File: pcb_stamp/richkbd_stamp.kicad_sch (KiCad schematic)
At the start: 48 parts, among them J1 USB_C_Receptacle, J2 OLED, K0 key-diode-led, K1 key-diode-led, K10 key-diode-led, K100 key-diode-led, K101 key-diode-led, K102 key-diode-led, K11 key-diode-led, K110 key-diode-led, K111 key-diode-led, K112 key-diode-led, K12 key-diode-led, K2 key-diode-led, K20 key-diode-led, K21 key-diode-led, K22 key-diode-led, K30 key-diode-led, K31 key-diode-led, K32 key-diode-led, K33 key-diode-led, K40 key-diode-led, K41 key-diode-led, K42 key-diode-led, K43 key-diode-led, K50 key-diode-led, K51 key-diode-led, K52 key-diode-led, K53 key-diode-led, K60 key-diode-led, K61 key-diode-led, K62 key-diode-led, K63 key-diode-led, K70 key-diode-led, K71 key-diode-led, K72 key-diode-led, K73 key-diode-led, K80 key-diode-led, K81 key-diode-led, K82 key-diode-led, K83 key-diode-led, K90 key-diode-led, K91 key-diode-led, K92 key-diode-led, U1 RP2040_Stamp

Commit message: Finished stamp routing
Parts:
- removed J1: USB_C_Receptacle, symbol Connector:USB_C_Receptacle
- added J1: USB_C_Receptacle_USB2.0, Connector_USB:USB_C_Receptacle_GCT_USB4085, symbol Connector:USB_C_Receptacle_USB2.0
- added R3, R4: R, Resistor_SMD:R_0805_2012Metric, symbol Device:R
- R1, R2: footprint kbd:R -> Resistor_SMD:R_0805_2012Metric
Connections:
- net GND: now also J1.A1 (GND), J1.A12 (GND), J1.B1 (GND), J1.B12 (GND), J1.S1 (SHIELD), R3.1, R4.1
- net LED: now also U1.15 (GPIO14)
- net SCL: now also U1.2 (GPIO1)
- net SDA: now also U1.1 (GPIO0)
- net VCC: now also J1.A4 (VBUS), J1.A9 (VBUS), J1.B4 (VBUS), J1.B9 (VBUS)
- net col0: now also U1.11 (GPIO10)
- net col1: now also U1.10 (GPIO9)
- net col10: now also U1.22 (GPIO21)
- net col11: now also U1.21 (GPIO20)
- net col2: now also U1.9 (GPIO8)
- net col3: now also U1.8 (GPIO7)
- net col4: now also U1.7 (GPIO6)
- net col5: now also U1.6 (GPIO5)
- net col6: now also U1.26 (GPIO25)
- net col7: now also U1.25 (GPIO24)
- net col8: now also U1.24 (GPIO23)
- net col9: now also U1.23 (GPIO22)
- net row0: now also U1.3 (GPIO2)
- net row1: now also U1.4 (GPIO3)
- net row2: now also U1.5 (GPIO4)
- net at U1.36 (USB_D+): now also J1.A6 (D+), J1.B6 (D+)
- net at U1.35 (USB_D-): now also J1.A7 (D-), J1.B7 (D-)
- new net CC1: J1.A5 (CC1), R3.2
- new net CC2: J1.B5 (CC2), R4.2
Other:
- moved on the sheet: J2, R1, R2, RSW1, U1

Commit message: Moved OLED up and fixed pin orientation
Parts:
- RSW1: value RESET -> BOOTSEL
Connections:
- net reset renamed bootsel
- no-connect marks 2 -> 21
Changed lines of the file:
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@@
   (junction (at 186.69 109.22) (diameter 0) (color 0 0 0 0)
   )
+  (no_connect (at 271.78 92.71))
+  (no_connect (at 271.78 95.25))
+  (no_connect (at 271.78 97.79))
+  (no_connect (at 271.78 100.33))
+  (no_connect (at 243.84 127))
+  (no_connect (at 243.84 124.46))
+  (no_connect (at 246.38 40.64))
+  (no_connect (at 271.78 54.61))
+  (no_connect (at 271.78 57.15))
+  (no_connect (at 271.78 59.69))
+  (no_connect (at 271.78 64.77))
+  (no_connect (at 271.78 67.31))
+  (no_connect (at 271.78 69.85))
+  (no_connect (at 271.78 72.39))
+  (no_connect (at 271.78 74.93))
+  (no_connect (at 246.38 57.15))
+  (no_connect (at 246.38 54.61))
+  (no_connect (at 246.38 31.75))
+  (no_connect (at 246.38 29.21))
   (no_connect (at 21.59 154.94))
   (no_connect (at 33.02 99.06))
@@
     )
   )
-  (global_label "reset" (shape input) (at 135.89 191.77 180) (fields_autoplaced)
+  (global_label "bootsel" (shape input) (at 135.89 191.77 180) (fields_autoplaced)
     (effects (font (size 1.524 1.524)) (justify right))
-    (property "Intersheet References" "${INTERSHEET_REFS}" (id 0) (at 101.6 107.95 0)
-      (effects (font (size 1.27 1.27)) hide)
+    (property "Intersheet References" "${INTERSHEET_REFS}" (id 0) (at 124.7554 191.6748 0)
+      (effects (font (size 1.524 1.524)) (justify right) hide)
     )
   )
@@
     )
   )
-  (global_label "reset" (shape input) (at 246.38 36.83 180) (fields_autoplaced)
+  (global_label "bootsel" (shape input) (at 246.38 36.83 180) (fields_autoplaced)
     (effects (font (size 1.524 1.524)) (justify right))
-    (property "Intersheet References" "${INTERSHEET_REFS}" (id 0) (at 212.09 -46.99 0)
-      (effects (font (size 1.27 1.27)) hide)
+    (property "Intersheet References" "${INTERSHEET_REFS}" (id 0) (at 235.2454 36.7348 0)
+      (effects (font (size 1.524 1.524)) (justify right) hide)
     )
   )
@@
     (in_bom yes) (on_board yes)
     (property "Reference" "RSW1" (id 0) (at 147.32 188.976 0))
-    (property "Value" "RESET" (id 1) (at 143.51 193.802 0))
+    (property "Value" "BOOTSEL" (id 1) (at 143.51 193.802 0))
     (property "Footprint" "kbd:ResetSW" (id 2) (at 143.51 191.77 0)
       (effects (font (size 1.27 1.27)) hide)
@@
     )
     (path "/00000000-0000-0000-0000-00005a5eb9e2"
-      (reference "RSW1") (unit 1) (value "RESET") (footprint "kbd:ResetSW")
+      (reference "RSW1") (unit 1) (value "BOOTSEL") (footprint "kbd:ResetSW")
     )
     (path "/262eff6c-faf0-42b5-906e-c377cdedb43d"

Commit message: Connected row3
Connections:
- net row3: now also U1.20 (GPIO19)
- no-connect marks 21 -> 20
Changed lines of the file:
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@@
   (no_connect (at 271.78 69.85))
   (no_connect (at 271.78 72.39))
-  (no_connect (at 271.78 74.93))
   (no_connect (at 246.38 57.15))
   (no_connect (at 246.38 54.61))
@@
       (effects (font (size 1.524 1.524)) (justify left) hide)
     )
+  )
+  (global_label "row3" (shape input) (at 271.78 74.93 0) (fields_autoplaced)
+    (effects (font (size 1.524 1.524)) (justify left))
+    (property "Intersheet References" "${INTERSHEET_REFS}" (id 0) (at 279.9392 74.8348 0)
+      (effects (font (size 1.524 1.524)) (justify left) hide)
+    )

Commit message: Start of rev2
Moved stamp to back
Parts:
- added RSW2: RESET, kbd:ResetSW, symbol corne-chocolate-rescue:SW_PUSH-kbd
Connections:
- net GND: now also RSW2.2
- net col0: now also U1.21 (GPIO20); no longer U1.11 (GPIO10)
- net col1: now also U1.22 (GPIO21); no longer U1.10 (GPIO9)
- net col10: now also U1.10 (GPIO9); no longer U1.22 (GPIO21)
- net col11: now also U1.11 (GPIO10); no longer U1.21 (GPIO20)
- net col2: now also U1.23 (GPIO22); no longer U1.9 (GPIO8)
- net col3: now also U1.24 (GPIO23); no longer U1.8 (GPIO7)
- net col4: now also U1.25 (GPIO24); no longer U1.7 (GPIO6)
- net col5: now also U1.26 (GPIO25); no longer U1.6 (GPIO5)
- net col6: now also U1.6 (GPIO5); no longer U1.26 (GPIO25)
- net col7: now also U1.7 (GPIO6); no longer U1.25 (GPIO24)
- net col8: now also U1.8 (GPIO7); no longer U1.24 (GPIO23)
- net col9: now also U1.9 (GPIO8); no longer U1.23 (GPIO22)
- net reset: now reaches U1.39 (~{RESET})
- net reset: now also RSW2.1
- no-connect marks 20 -> 19
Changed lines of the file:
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@@
   (no_connect (at 243.84 127))
   (no_connect (at 243.84 124.46))
-  (no_connect (at 246.38 40.64))
   (no_connect (at 271.78 54.61))
   (no_connect (at 271.78 57.15))
@@
     (stroke (width 0) (type default) (color 0 0 0 0))
   )
-  (global_label "col8" (shape input) (at 271.78 85.09 0) (fields_autoplaced)
+  (global_label "col8" (shape input) (at 271.78 44.45 0) (fields_autoplaced)
     (effects (font (size 1.524 1.524)) (justify left))
-    (property "Intersheet References" "${INTERSHEET_REFS}" (id 0) (at 279.5038 84.9948 0)
+    (property "Intersheet References" "${INTERSHEET_REFS}" (id 0) (at 279.5038 44.3548 0)
       (effects (font (size 1.524 1.524)) (justify left) hide)
     )
@@
     )
   )
-  (global_label "col10" (shape input) (at 271.78 80.01 0) (fields_autoplaced)
+  (global_label "col10" (shape input) (at 271.78 49.53 0) (fields_autoplaced)
     (effects (font (size 1.524 1.524)) (justify left))
-    (property "Intersheet References" "${INTERSHEET_REFS}" (id 0) (at 280.9552 79.9148 0)
+    (property "Intersheet References" "${INTERSHEET_REFS}" (id 0) (at 280.9552 49.4348 0)
       (effects (font (size 1.524 1.524)) (justify left) hide)
     )
@@
     )
   )
-  (global_label "col3" (shape input) (at 271.78 44.45 0) (fields_autoplaced)
+  (global_label "col3" (shape input) (at 271.78 85.09 0) (fields_autoplaced)
     (effects (font (size 1.524 1.524)) (justify left))
-    (property "Intersheet References" "${INTERSHEET_REFS}" (id 0) (at 279.5038 44.3548 0)
+    (property "Intersheet References" "${INTERSHEET_REFS}" (id 0) (at 279.5038 84.9948 0)
       (effects (font (size 1.524 1.524)) (justify left) hide)
     )
@@
     )
   )
-  (global_label "col7" (shape input) (at 271.78 87.63 0) (fields_autoplaced)
+  (global_label "col7" (shape input) (at 271.78 41.91 0) (fields_autoplaced)
     (effects (font (size 1.524 1.524)) (justify left))
-    (property "Intersheet References" "${INTERSHEET_REFS}" (id 0) (at 279.5038 87.5348 0)
+    (property "Intersheet References" "${INTERSHEET_REFS}" (id 0) (at 279.5038 41.8148 0)
       (effects (font (size 1.524 1.524)) (justify left) hide)
     )
@@
     )
   )
-  (global_label "col11" (shape input) (at 271.78 77.47 0) (fields_autoplaced)
+  (global_label "col11" (shape input) (at 271.78 52.07 0) (fields_autoplaced)
     (effects (font (size 1.524 1.524)) (justify left))
-    (property "Intersheet References" "${INTERSHEET_REFS}" (id 0) (at 280.9552 77.3748 0)
+    (property "Intersheet References" "${INTERSHEET_REFS}" (id 0) (at 280.9552 51.9748 0)
       (effects (font (size 1.524 1.524)) (justify left) hide)
     )
@@
     )
   )
-  (global_label "col1" (shape input) (at 271.78 49.53 0) (fields_autoplaced)
+  (global_label "col1" (shape input) (at 271.78 80.01 0) (fields_autoplaced)
     (effects (font (size 1.524 1.524)) (justify left))
-    (property "Intersheet References" "${INTERSHEET_REFS}" (id 0) (at 279.5038 49.4348 0)
+    (property "Intersheet References" "${INTERSHEET_REFS}" (id 0) (at 279.5038 79.9148 0)
       (effects (font (size 1.524 1.524)) (justify left) hide)
     )
@@
     )
   )
-  (global_label "col0" (shape input) (at 271.78 52.07 0) (fields_autoplaced)
+  (global_label "col0" (shape input) (at 271.78 77.47 0) (fields_autoplaced)
     (effects (font (size 1.524 1.524)) (justify left))
-    (property "Intersheet References" "${INTERSHEET_REFS}" (id 0) (at 279.5038 51.9748 0)
+    (property "Intersheet References" "${INTERSHEET_REFS}" (id 0) (at 279.5038 77.3748 0)
       (effects (font (size 1.524 1.524)) (justify left) hide)
     )
@@
     )
   )
-  (global_label "col9" (shape input) (at 271.78 82.55 0) (fields_autoplaced)
+  (global_label "col9" (shape input) (at 271.78 46.99 0) (fields_autoplaced)
     (effects (font (size 1.524 1.524)) (justify left))
-    (property "Intersheet References" "${INTERSHEET_REFS}" (id 0) (at 279.5038 82.4548 0)
+    (property "Intersheet References" "${INTERSHEET_REFS}" (id 0) (at 279.5038 46.8948 0)
       (effects (font (size 1.524 1.524)) (justify left) hide)
     )
@@
     )
   )
-  (global_label "col5" (shape input) (at 271.78 39.37 0) (fields_autoplaced)
+  (global_label "col5" (shape input) (at 271.78 90.17 0) (fields_autoplaced)
     (effects (font (size 1.524 1.524)) (justify left))
-    (property "Intersheet References" "${INTERSHEET_REFS}" (id 0) (at 279.5038 39.2748 0)
+    (property "Intersheet References" "${INTERSHEET_REFS}" (id 0) (at 279.5038 90.0748 0)
       (effects (font (size 1.524 1.524)) (justify left) hide)
     )
@@
     )
   )
-  (global_label "col4" (shape input) (at 271.78 41.91 0) (fields_autoplaced)
+  (global_label "col4" (shape input) (at 271.78 87.63 0) (fields_autoplaced)
     (effects (font (size 1.524 1.524)) (justify left))
-    (property "Intersheet References" "${INTERSHEET_REFS}" (id 0) (at 279.5038 41.8148 0)
+    (property "Intersheet References" "${INTERSHEET_REFS}" (id 0) (at 279.5038 87.5348 0)
       (effects (font (size 1.524 1.524)) (justify left) hide)
     )
@@
     )
   )
+  (global_label "reset" (shape input) (at 104.14 192.405 180) (fields_autoplaced)
+    (effects (font (size 1.524 1.524)) (justify right))
+    (property "Intersheet References" "${INTERSHEET_REFS}" (id 0) (at 95.6905 192.3098 0)
+      (effects (font (size 1.524 1.524)) (justify right) hide)
+    )
+  )
   (global_label "row0" (shape input) (at 128.27 109.22 180) (fields_autoplaced)
     (effects (font (size 1.524 1.524)) (justify right))
@@
     )
   )
+  (global_label "reset" (shape input) (at 246.38 41.91 180) (fields_autoplaced)
+    (effects (font (size 1.524 1.524)) (justify right))
+    (property "Intersheet References" "${INTERSHEET_REFS}" (id 0) (at 237.9305 41.8148 0)
+      (effects (font (size 1.524 1.524)) (justify right) hide)
+    )
+  )
   (global_label "row0" (shape input) (at 57.15 30.48 180) (fields_autoplaced)
     (effects (font (size 1.524 1.524)) (justify right))
@@
     )
   )
-  (global_label "col6" (shape input) (at 271.78 90.17 0) (fields_autoplaced)
+  (global_label "col6" (shape input) (at 271.78 39.37 0) (fields_autoplaced)
     (effects (font (size 1.524 1.524)) (justify left))
-    (property "Intersheet References" "${INTERSHEET_REFS}" (id 0) (at 279.5038 90.0748 0)
+    (property "Intersheet References" "${INTERSHEET_REFS}" (id 0) (at 279.5038 39.2748 0)
       (effects (font (size 1.524 1.524)) (justify left) hide)
     )
@@
     )
   )
-  (global_label "col2" (shape input) (at 271.78 46.99 0) (fields_autoplaced)
+  (global_label "col2" (shape input) (at 271.78 82.55 0) (fields_autoplaced)
     (effects (font (size 1.524 1.524)) (justify left))
-    (property "Intersheet References" "${INTERSHEET_REFS}" (id 0) (at 279.5038 46.8948 0)
+    (property "Intersheet References" "${INTERSHEET_REFS}" (id 0) (at 279.5038 82.4548 0)
       (effects (font (size 1.524 1.524)) (justify left) hide)
     )
@@
     (pin "1")
   )
+  (symbol (lib_id "power:GND") (at 119.38 192.405 0) (unit 1)
+    (in_bom yes) (on_board yes)
+    (property "Reference" "#PWR?" (id 0) (at 119.38 198.755 0)
+      (effects (font (size 1.27 1.27)) hide)
+    )
+    (property "Value" "GND" (id 1) (at 119.38 196.215 0))
+    (property "Footprint" "" (id 2) (at 119.38 192.405 0)
+      (effects (font (size 1.27 1.27)) hide)
+    )
+    (property "Datasheet" "" (id 3) (at 119.38 192.405 0)
+      (effects (font (size 1.27 1.27)) hide)
+    )
+    (pin "1")
+  )
   (symbol (lib_id "nashlib:key-diode-led") (at 168.91 60.96 0) (unit 1)
     (in_bom yes) (on_board yes) (fields_autoplaced)
@@
     (pin "1")
   )
+  (symbol (lib_id "corne-chocolate-rescue:SW_PUSH-kbd") (at 111.76 192.405 0) (unit 1)
+    (in_bom yes) (on_board yes)
+    (property "Reference" "RSW2" (id 0) (at 115.57 189.611 0))
+    (property "Value" "RESET" (id 1) (at 111.76 194.437 0))
+    (property "Footprint" "kbd:ResetSW" (id 2) (at 111.76 192.405 0)
+      (effects (font (size 1.27 1.27)) hide)
+    )
+    (property "Datasheet" "" (id 3) (at 111.76 192.405 0))
+    (pin "1")
+    (pin "2")
+  )
   (symbol (lib_name "key-diode-led_17") (lib_id "nashlib:key-diode-led") (at 62.23 106.68 0) (unit 1)
     (in_bom yes) (on_board yes) (fields_autoplaced)
@@
       (reference "#PWR0196") (unit 1) (value "GND") (footprint "")
     )
+    (path "/8e04b2ad-ebd4-4324-ad5e-d1232b9f4b86"
+      (reference "#PWR?") (unit 1) (value "GND") (footprint "")
+    )
     (path "/47635ebf-71db-4bb1-8e53-065bacc076fa"
       (reference "J1") (unit 1) (value "USB_C_Receptacle_USB2.0") (footprint "Connector_USB:USB_C_Receptacle_GCT_USB4085")
@@
       (reference "RSW1") (unit 1) (value "BOOTSEL") (footprint "kbd:ResetSW")
     )
+    (path "/e2d7f888-cbbd-4e31-927c-7b725502298a"
+      (reference "RSW2") (unit 1) (value "RESET") (footprint "kbd:ResetSW")
+    )
     (path "/262eff6c-faf0-42b5-906e-c377cdedb43d"

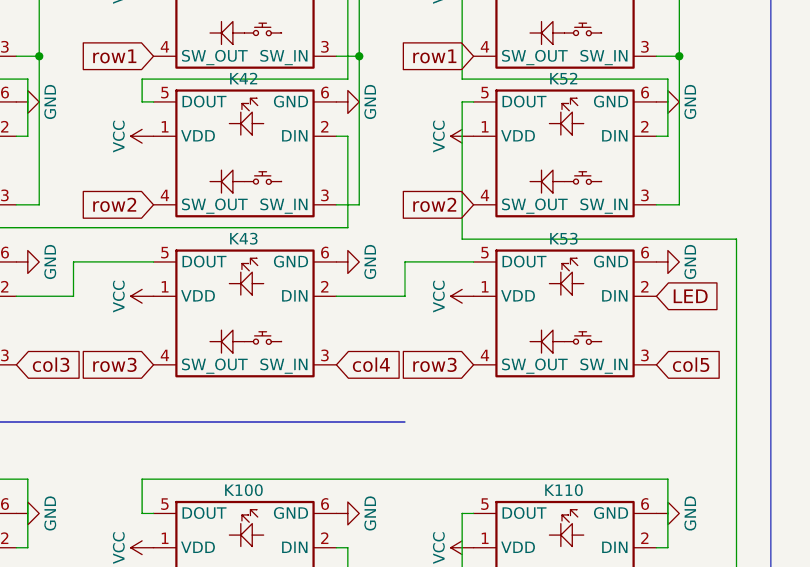
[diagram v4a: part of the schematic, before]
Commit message: Added diode on first LED pixel power pin to bring it into spec for the rp2040's 3.3V logic
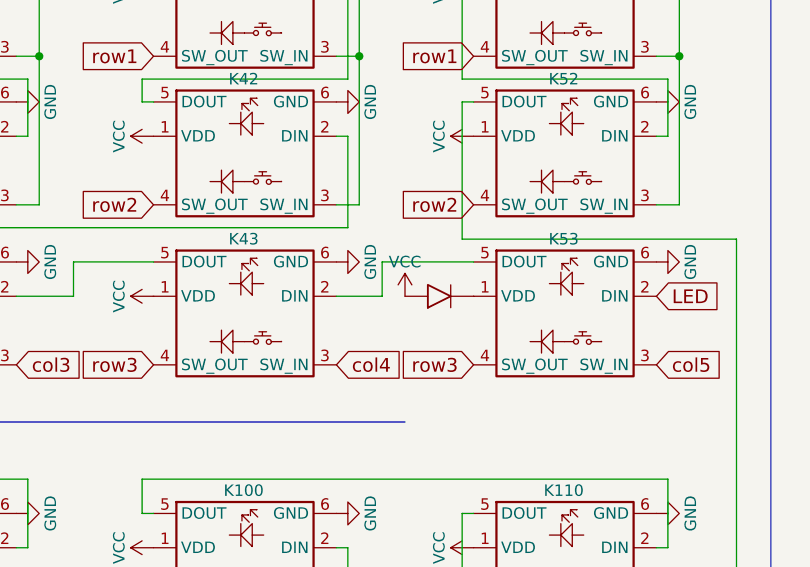
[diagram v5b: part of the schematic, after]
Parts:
- added D1: 1N914BWS, Diode_SMD:D_1812_4532Metric_Pad1.30x3.40mm_HandSolder, symbol 4ms_Diode:1N914BWS
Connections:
- net VCC: now also D1.2 (A); no longer K53.1 (VDD)
- new net: D1.1 (K), K53.1 (VDD)
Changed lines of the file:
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@@
     (stroke (width 0) (type default) (color 0 0 0 0))
   )
-  (wire (pts (xy 191.77 73.66) (xy 184.15 73.66))
+  (wire (pts (xy 189.23 73.66) (xy 184.15 73.66))
     (stroke (width 0) (type default) (color 0 0 0 0))
   )
@@
     (stroke (width 0) (type default) (color 0 0 0 0))
   )
-  (wire (pts (xy 191.77 69.85) (xy 191.77 73.66))
+  (wire (pts (xy 189.23 69.85) (xy 189.23 73.66))
     (stroke (width 0) (type default) (color 0 0 0 0))
   )
@@
     (stroke (width 0) (type default) (color 0 0 0 0))
   )
-  (wire (pts (xy 199.39 69.85) (xy 191.77 69.85))
+  (wire (pts (xy 199.39 69.85) (xy 189.23 69.85))
     (stroke (width 0) (type default) (color 0 0 0 0))
   )
@@
     (pin "1")
   )
+  (symbol (lib_id "4ms_Diode:1N914BWS") (at 195.58 73.66 180) (unit 1)
+    (in_bom yes) (on_board yes) (fields_autoplaced)
+    (property "Reference" "D1" (id 0) (at 195.58 80.01 0)
+      (effects (font (size 1.27 1.27)) hide)
+    )
+    (property "Value" "1N914BWS" (id 1) (at 195.58 71.12 0)
+      (effects (font (size 1.27 1.27)) hide)
+    )
+    (property "Footprint" "Diode_SMD:D_1812_4532Metric_Pad1.30x3.40mm_HandSolder" (id 2) (at 195.58 78.74 0)
+      (effects (font (size 1.27 1.27)) hide)
+    )
+    (property "Datasheet" "https://www.mouser.com/datasheet/2/308/1N914BWS_D-2309364.pdf" (id 3) (at 195.58 73.66 0)
+      (effects (font (size 1.27 1.27)) hide)
+    )
+    (property "Specifications" "1N914BWS, 75V, 150mA, 1V @ 100mA SOD-323F" (id 4) (at 198.12 65.786 0)
+      (effects (font (size 1.27 1.27)) (justify left) hide)
+    )
+    (property "Manufacturer" "ON Semiconductor / Fairchild" (id 5) (at 198.12 64.262 0)
+      (effects (font (size 1.27 1.27)) (justify left) hide)
+    )
+    (property "Part Number" "1N914BWS" (id 6) (at 198.12 62.738 0)
+      (effects (font (size 1.27 1.27)) (justify left) hide)
+    )
+    (property "JLCPCB ID" "C258181" (id 7) (at 198.12 62.738 0)
+      (effects (font (size 1.27 1.27)) (justify left) hide)
+    )
+    (property "Display" "1N914" (id 8) (at 195.58 77.47 0)
+      (effects (font (size 1.27 1.27)) hide)
+    )
+    (pin "1")
+    (pin "2")
+  )
   (symbol (lib_id "power:VCC") (at 163.83 39.37 90) (unit 1)
     (in_bom yes) (on_board yes)
@@
     (pin "1")
   )
-  (symbol (lib_id "power:VCC") (at 199.39 73.66 90) (unit 1)
+  (symbol (lib_id "power:VCC") (at 191.77 73.66 0) (unit 1)
     (in_bom yes) (on_board yes)
-    (property "Reference" "#PWR0114" (id 0) (at 203.2 73.66 0)
+    (property "Reference" "#PWR0114" (id 0) (at 191.77 77.47 0)
       (effects (font (size 1.27 1.27)) hide)
     )
-    (property "Value" "VCC" (id 1) (at 195.58 73.66 0))
-    (property "Footprint" "" (id 2) (at 199.39 73.66 0)
+    (property "Value" "VCC" (id 1) (at 191.77 69.85 0))
+    (property "Footprint" "" (id 2) (at 191.77 73.66 0)
       (effects (font (size 1.27 1.27)) hide)
     )
-    (property "Datasheet" "" (id 3) (at 199.39 73.66 0)
+    (property "Datasheet" "" (id 3) (at 191.77 73.66 0)
       (effects (font (size 1.27 1.27)) hide)
     )
@@
       (reference "#PWR?") (unit 1) (value "GND") (footprint "")
     )
+    (path "/5530f26f-ed7b-4419-9257-0a8f680475f6"
+      (reference "D1") (unit 1) (value "1N914BWS") (footprint "Diode_SMD:D_1812_4532Metric_Pad1.30x3.40mm_HandSolder")
+    )
     (path "/47635ebf-71db-4bb1-8e53-065bacc076fa"
